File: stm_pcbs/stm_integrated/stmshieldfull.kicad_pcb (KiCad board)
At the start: 2 copper layers, 177 parts, among them P1 BNC, P2 BNC, P3 BNC, P4 BNC, P5 BNC, U1 AD8676, U10 AD8676, U11 AD5791, U12 AD8675, U13 AD8676, U14 AD8675, U15 ADR445, U16 LT1019ACS8, U17 LTC1859, U2 AD5791, U3 AD8675, U4 AD8676, U5 AD5791, U6 AD8675, U7 AD8676, U8 AD5791, U9 AD8675

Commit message: working on Kicad of 3rd Dec
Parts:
- added P6: CONN_20X2, Connectors_IDC:IDC-Header_2x20_Pitch2.54mm_Straight, F.Cu at (127.8, 64.2)
- moved U9 73.9 mm to (-17.3, 158.7)
- moved C7 73.9 mm to (-41.3, 154.8)
- moved U8 73.9 mm to (-15.0, 148.4)
- moved C12 73.9 mm to (-37.6, 147.6)
- moved P3 73.9 mm to (-24.8, 157.8)
- moved R1 73.9 mm to (-41.3, 148.4)
- moved C71 61.8 mm to (209.9, 65.8)
- moved C73 61.8 mm to (208.9, 61.8)
- moved R6 61.8 mm to (203.9, 67.8)
- moved R9 61.8 mm to (195.9, 90.0)
- moved C65 61.8 mm to (201.9, 89.8)
- moved C66 61.8 mm to (189.9, 83.8)
- moved C67 61.8 mm to (204.9, 88.8)
- moved C68 61.8 mm to (185.9, 82.8)
- moved C69 61.8 mm to (198.4, 71.3)
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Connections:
- C10 pad 2: -14V -> Net-(C10-Pad2)
- C14 pad 2: -14V -> Net-(C14-Pad2)
- C16 pad 1: -14V -> Net-(C16-Pad1)
- C18 pad 1: 3.3V -> Net-(C18-Pad1)
- C19 pad 2: +14V -> Net-(C19-Pad2)
- C2 pad 1: 3.3V -> Net-(C2-Pad1)
- C25 pad 1: +14V -> Net-(C25-Pad1)
- C25 pad 2: AGND -> Net-(C25-Pad2)
- C26 pad 2: -14V -> Net-(C26-Pad2)
- C3 pad 2: +14V -> Net-(C3-Pad2)
- C30 pad 2: -14V -> Net-(C30-Pad2)
- C32 pad 1: -14V -> Net-(C32-Pad1)
- C34 pad 1: 3.3V -> Net-(C34-Pad1)
- C35 pad 2: +14V -> Net-(C35-Pad2)
- C41 pad 1: +14V -> Net-(C41-Pad1)
- C41 pad 2: AGND -> Net-(C41-Pad2)
- C42 pad 2: -14V -> Net-(C42-Pad2)
- C46 pad 2: -14V -> Net-(C46-Pad2)
- C48 pad 1: -14V -> Net-(C48-Pad1)
- C50 pad 1: 3.3V -> Net-(C50-Pad1)
- C51 pad 2: +14V -> Net-(C51-Pad2)
- C57 pad 1: +14V -> Net-(C57-Pad1)
- C57 pad 2: AGND -> Net-(C57-Pad2)
- C58 pad 2: -14V -> Net-(C58-Pad2)
- C62 pad 2: -14V -> Net-(C62-Pad2)
- C64 pad 1: -14V -> Net-(C64-Pad1)
- C71 pad 2: -14V -> Net-(C71-Pad2)
- C72 pad 1: +14V -> Net-(C72-Pad1)
- C72 pad 2: AGND -> Net-(C72-Pad2)
- C74 pad 1: +15V -> Net-(C74-Pad1)
- C74 pad 2: GND -> DGND
- C75 pad 2: GND -> Net-(C75-Pad2)
- C76 pad 2: GND -> Net-(C76-Pad2)
- C80 pad 2: AGND -> Net-(C80-Pad2)
- C81 pad 1: +5V -> Net-(C81-Pad1)
- C82 pad 1: +5V -> Net-(C82-Pad1)
- C9 pad 1: +14V -> Net-(C9-Pad1)
- C9 pad 2: AGND -> Net-(C9-Pad2)
- P5 pad 1: Net-(C78-Pad1) -> Net-(P5-Pad1)
- R10 pad 2: AGND -> Net-(R10-Pad2)
- R5 pad 1: Net-(C69-Pad1) -> Net-(R5-Pad1)
- R5 pad 2: 5VREF -> Net-(R5-Pad2)
- R8 pad 1: +10VREF -> Net-(R8-Pad1)
- R8 pad 2: Net-(R6-Pad1) -> Net-(R8-Pad2)
- R9 pad 1: -10VREF -> Net-(R9-Pad1)
- R9 pad 2: Net-(R7-Pad1) -> Net-(R9-Pad2)
- U11 pad 14: (no net) -> SYNC4
- U11 pad 6: (no net) -> RESET4
- U11 pad 7: (no net) -> CLR4
- U11 pad 8: (no net) -> LDAC4
- U13 pad 1: Net-(R7-Pad2) -> Net-(U13-Pad1)
- U13 pad 2: Net-(R7-Pad2) -> Net-(U13-Pad1)
- U13 pad 3: Net-(C69-Pad1) -> Net-(U13-Pad3)
- U13 pad 6: Net-(R7-Pad1) -> Net-(U13-Pad6)
- U14 pad 3: Net-(C69-Pad1) -> Net-(U13-Pad3)
- U15 pad 1: (no net) -> Net-(U15-Pad1)
- U15 pad 3: (no net) -> Net-(U15-Pad3)
- U15 pad 4: GND -> DGND
- U15 pad 5: (no net) -> Net-(U15-Pad5)
- U15 pad 7: (no net) -> Net-(U15-Pad7)
- U15 pad 8: (no net) -> Net-(U15-Pad8)
- U16 pad 1: (no net) -> Net-(U16-Pad1)
- U16 pad 3: (no net) -> Net-(U16-Pad3)
- U16 pad 5: (no net) -> Net-(U16-Pad5)
- U16 pad 6: Net-(C79-Pad1) -> Net-(U16-Pad6)
- U16 pad 7: (no net) -> Net-(U16-Pad7)
- U16 pad 8: (no net) -> Net-(U16-Pad8)
- U17 pad 15: Net-(C79-Pad1) -> Net-(U16-Pad6)
- U17 pad 16: Net-(C80-Pad1) -> Net-(U17-Pad16)
- U17 pad 2: Net-(C78-Pad1) -> Net-(P5-Pad1)
- U17 pad 22: (no net) -> ADC_BUSY
- U17 pad 23: (no net) -> SDO
- U17 pad 25: (no net) -> SDIN
- U17 pad 26: (no net) -> SCLK
- U17 pad 27: (no net) -> ADC_RD
- U17 pad 28: (no net) -> ADC_CONVST
- U17 pad 3: (no net) -> Net-(U17-Pad3)
- U17 pad 4: (no net) -> Net-(U17-Pad4)
- U17 pad 5: (no net) -> Net-(U17-Pad5)
- U17 pad 6: (no net) -> Net-(U17-Pad6)
- U17 pad 7: (no net) -> Net-(U17-Pad7)
- U17 pad 8: (no net) -> Net-(U17-Pad8)
- U17 pad 9: (no net) -> Net-(U17-Pad9)
- U2 pad 14: (no net) -> SYNC2
- U2 pad 6: (no net) -> RESET2
- U2 pad 7: (no net) -> CLR2
- U2 pad 8: (no net) -> LDAC2
- U5 pad 14: (no net) -> SYNC1
- U5 pad 6: (no net) -> RESET1
- U5 pad 7: (no net) -> CLR1
- U5 pad 8: (no net) -> LDAC1
- U8 pad 14: (no net) -> SYNC3
- U8 pad 6: (no net) -> RESET3
- U8 pad 7: (no net) -> CLR3
- U8 pad 8: (no net) -> LDAC3
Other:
- board outline added: 148.6 x 101.3 mm

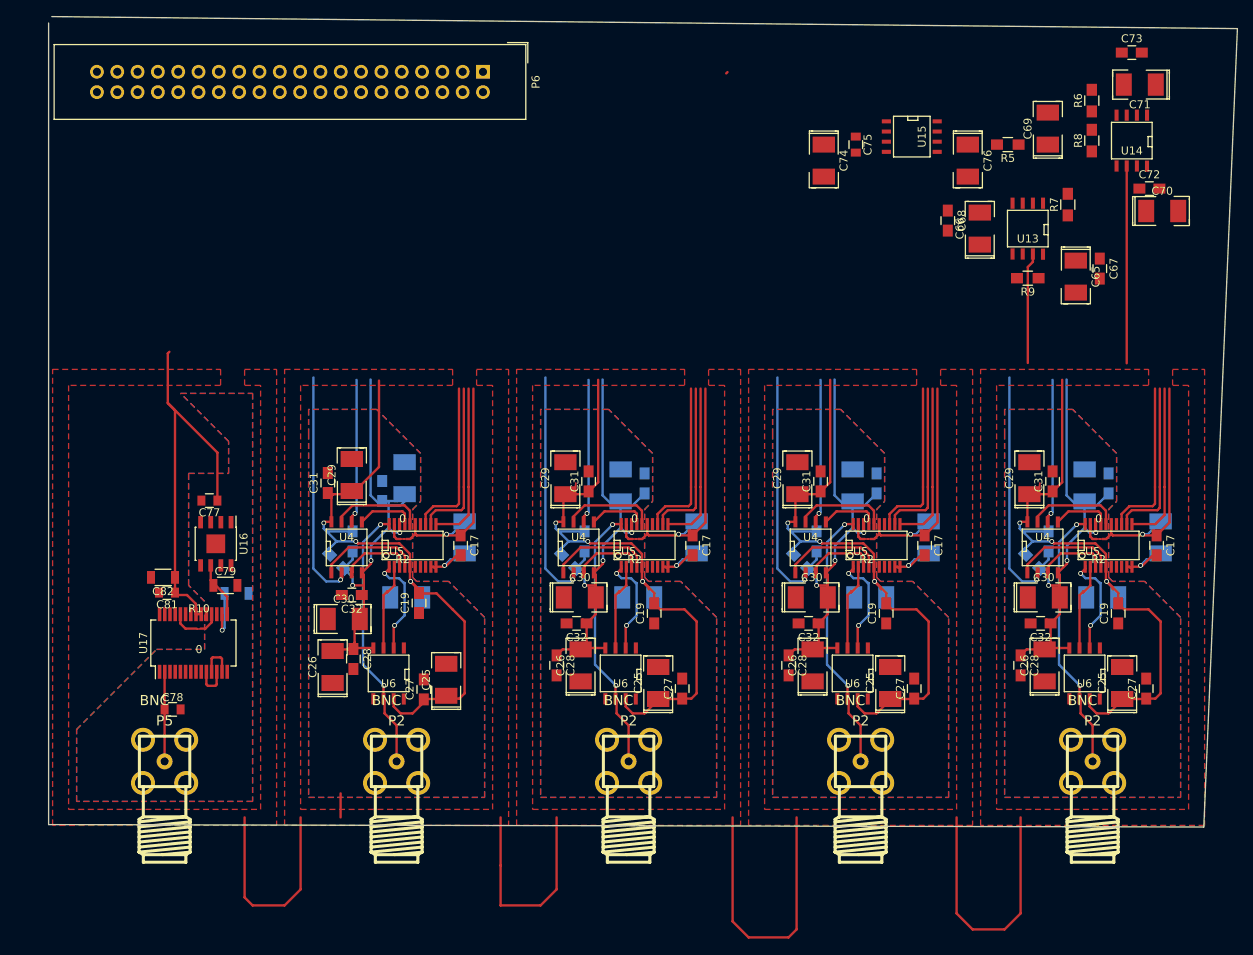
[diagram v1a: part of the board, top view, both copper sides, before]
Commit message: tidying up boards, adding all DAC signals.
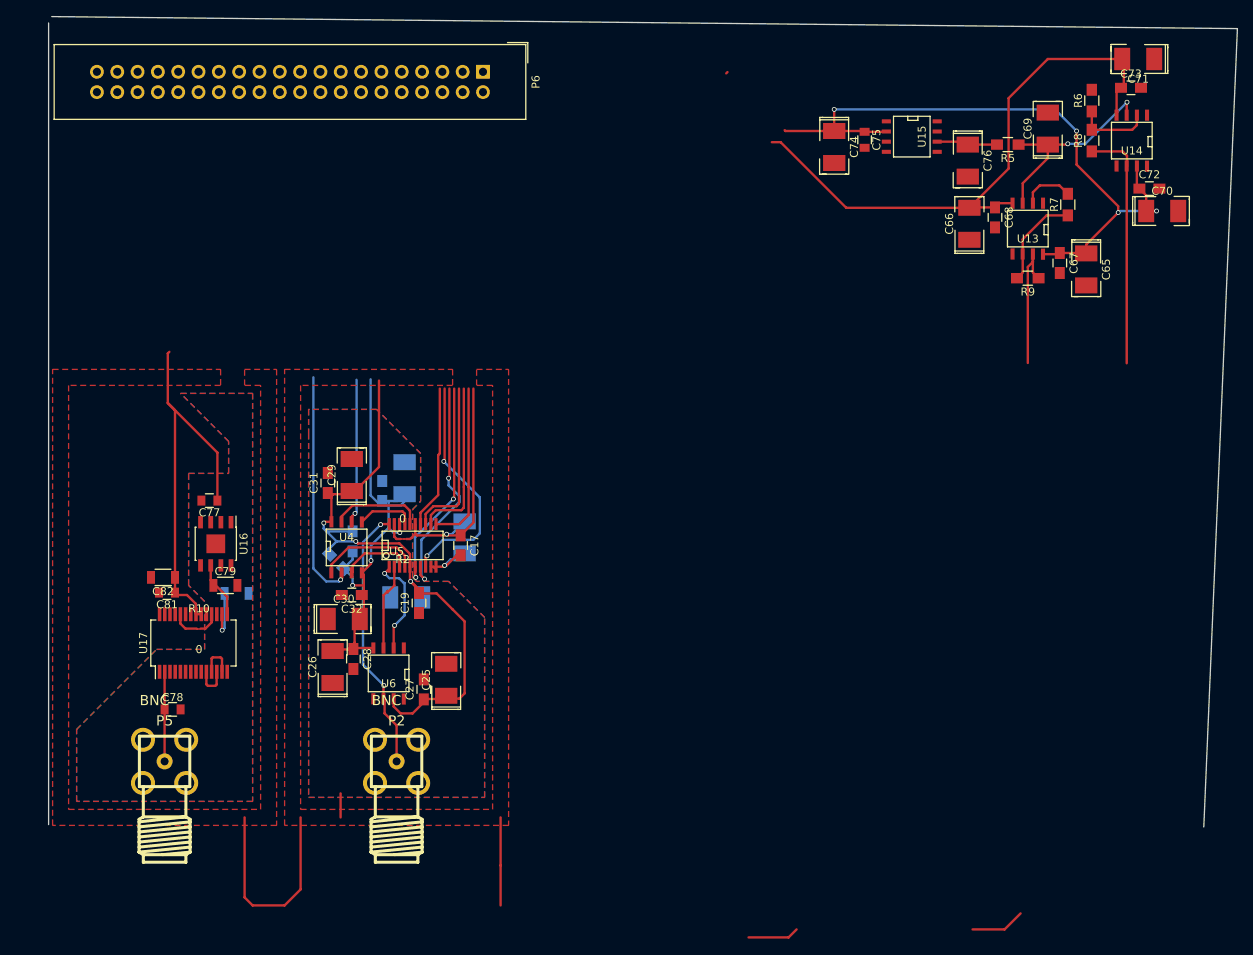
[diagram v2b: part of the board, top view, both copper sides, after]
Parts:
- removed the C17 at (183.0, 123.4)
- removed the C17 at (212.0, 123.4)
- removed the C17 at (154.0, 123.4)
- removed the C18 at (183.5, 122.4)
- removed the C18 at (212.5, 122.4)
- removed the C18 at (154.5, 122.4)
- removed the C19 at (178.2, 131.9)
- removed the C19 at (207.2, 131.9)
- removed the C19 at (149.2, 131.9)
- removed the C20 at (176.2, 129.9)
- removed the C20 at (205.2, 129.9)
- removed the C20 at (147.2, 129.9)
- removed the C21 at (177.0, 115.6)
- removed the C21 at (206.0, 115.6)
- removed the C21 at (148.0, 115.6)
- removed the C22 at (174.0, 115.9)
- removed the C22 at (203.0, 115.9)
- removed the C22 at (145.0, 115.9)
- removed the C23 at (167.5, 125.4)
- removed the C23 at (196.5, 125.4)
- removed the C23 at (138.5, 125.4)
- removed the C24 at (169.5, 122.9)
- removed the C24 at (198.5, 122.9)
- removed the C24 at (140.5, 122.9)
- removed the C25 at (178.7, 140.6)
- removed the C25 at (207.7, 140.6)
- removed the C25 at (149.7, 140.6)
- removed the C26 at (169.0, 138.4)
- removed the C26 at (198.0, 138.4)
- removed the C26 at (140.0, 138.4)
- removed the C27 at (181.7, 141.3)
- removed the C27 at (210.7, 141.3)
- removed the C27 at (152.7, 141.3)
- removed the C28 at (166.0, 138.4)
- removed the C28 at (195.0, 138.4)
- removed the C28 at (137.0, 138.4)
- removed the C29 at (167.1, 115.0)
- removed the C29 at (196.1, 115.0)
- removed the C29 at (138.1, 115.0)
- removed the C30 at (168.9, 129.9)
- removed the C30 at (197.9, 129.9)
- removed the C30 at (139.9, 129.9)
- removed the C31 at (170.0, 115.4)
- removed the C31 at (199.0, 115.4)
- removed the C31 at (141.0, 115.4)
- removed the C32 at (168.5, 133.1)
- removed the C32 at (197.5, 133.1)
- removed the C32 at (139.5, 133.1)
- removed the P2 at (175.0, 150.4)
- removed the P2 at (204.0, 150.4)
- removed the P2 at (146.0, 150.4)
- removed the R2 at (175.7, 122.6)
- removed the R2 at (204.7, 122.6)
- removed the R2 at (146.7, 122.6)
- removed the U4 at (168.7, 123.6)
- removed the U4 at (197.7, 123.6)
- removed the U4 at (139.7, 123.6)
- removed the U5 at (177.0, 123.4)
- removed the U5 at (206.0, 123.4)
- removed the U5 at (148.0, 123.4)
- removed the U6 at (174.0, 139.4)
- removed the U6 at (203.0, 139.4)
- removed the U6 at (145.0, 139.4)
- moved C68 5.91 mm to (191.8, 82.4)
- moved C67 5.05 mm to (199.9, 88.1)
- moved C73 4.40 mm to (208.8, 66.2)
- moved C71 3.21 mm to (209.7, 62.6)
- moved C74 2.14 mm to (171.7, 73.6)
- moved C65 1.58 mm to (203.2, 88.9)
- moved C66 1.43 mm to (188.6, 83.2)
- moved C75 1.25 mm to (175.5, 72.7)
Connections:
- C1 pad 2: 3.3V -> +5V
- C10 pad 2: Net-(C10-Pad2) -> -14V
- C14 pad 2: Net-(C14-Pad2) -> -14V
- C16 pad 1: Net-(C16-Pad1) -> -14V
- C17 pad 2: 3.3V -> +5V
- C18 pad 1: 3.3V -> +5V
- C2 pad 1: Net-(C2-Pad1) -> +5V
- C3 pad 2: Net-(C3-Pad2) -> +14V
- C30 pad 2: -14V -> Net-(C30-Pad2)
- C32 pad 1: -14V -> Net-(C32-Pad1)
- C33 pad 2: 3.3V -> +5V
- C34 pad 1: Net-(C34-Pad1) -> +5V
- C35 pad 2: Net-(C35-Pad2) -> +14V
- C41 pad 1: Net-(C41-Pad1) -> +14V
- C41 pad 2: Net-(C41-Pad2) -> AGND
- C42 pad 2: Net-(C42-Pad2) -> -14V
- C46 pad 2: Net-(C46-Pad2) -> -14V
- C48 pad 1: Net-(C48-Pad1) -> -14V
- C49 pad 2: 3.3V -> +5V
- C50 pad 1: Net-(C50-Pad1) -> +5V
- C51 pad 2: Net-(C51-Pad2) -> +14V
- C57 pad 1: Net-(C57-Pad1) -> +14V
- C57 pad 2: Net-(C57-Pad2) -> AGND
- C58 pad 2: Net-(C58-Pad2) -> -14V
- C62 pad 2: Net-(C62-Pad2) -> -14V
- C64 pad 1: Net-(C64-Pad1) -> -14V
- C71 pad 2: Net-(C71-Pad2) -> -14V
- C72 pad 1: Net-(C72-Pad1) -> +14V
- C72 pad 2: Net-(C72-Pad2) -> AGND
- C74 pad 1: Net-(C74-Pad1) -> +14V
- C74 pad 2: DGND -> AGND
- C75 pad 1: +15V -> +14V
- C75 pad 2: Net-(C75-Pad2) -> AGND
- C76 pad 2: Net-(C76-Pad2) -> AGND
- C80 pad 2: Net-(C80-Pad2) -> AGND
- C81 pad 1: Net-(C81-Pad1) -> +5V
- C82 pad 1: Net-(C82-Pad1) -> +5V
- C9 pad 1: Net-(C9-Pad1) -> +14V
- C9 pad 2: Net-(C9-Pad2) -> AGND
- P5 pad 1: Net-(P5-Pad1) -> Net-(C78-Pad1)
- R10 pad 2: Net-(R10-Pad2) -> AGND
- R5 pad 1: Net-(R5-Pad1) -> Net-(C69-Pad1)
- R5 pad 2: Net-(R5-Pad2) -> 5VREF
- R8 pad 1: Net-(R8-Pad1) -> +10VREF
- R8 pad 2: Net-(R8-Pad2) -> Net-(R6-Pad1)
- R9 pad 1: Net-(R9-Pad1) -> -10VREF
- R9 pad 2: Net-(R9-Pad2) -> Net-(R7-Pad1)
- U11 pad 10: 3.3V -> +5V
- U11 pad 9: 3.3V -> +5V
- U13 pad 1: Net-(U13-Pad1) -> Net-(R7-Pad2)
- U13 pad 2: Net-(U13-Pad1) -> Net-(R7-Pad2)
- U13 pad 3: Net-(U13-Pad3) -> Net-(C69-Pad1)
- U13 pad 6: Net-(U13-Pad6) -> Net-(R7-Pad1)
- U14 pad 3: Net-(U13-Pad3) -> Net-(C69-Pad1)
- U15 pad 2: +15V -> +14V
- U15 pad 4: DGND -> AGND
- U16 pad 6: Net-(U16-Pad6) -> Net-(C79-Pad1)
- U17 pad 15: Net-(U16-Pad6) -> Net-(C79-Pad1)
- U17 pad 16: Net-(U17-Pad16) -> Net-(C80-Pad1)
- U17 pad 2: Net-(P5-Pad1) -> Net-(C78-Pad1)
- U2 pad 10: 3.3V -> +5V
- U2 pad 9: 3.3V -> +5V
- U5 pad 10: 3.3V -> +5V
- U5 pad 14: (no net) -> SYNC1
- U5 pad 6: (no net) -> RESET1
- U5 pad 7: (no net) -> CLR1
- U5 pad 8: (no net) -> LDAC1
- U5 pad 9: 3.3V -> +5V
- U8 pad 10: 3.3V -> +5V
- U8 pad 9: 3.3V -> +5V
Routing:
- net +14V: track 317.4 -> 163.7 mm, vias 12 -> 7
- net -14V: track 237.6 -> 135.6 mm, vias 12 -> 3
- net Net-(P2-Pad1): track 133.5 -> 33.4 mm, vias 8 -> 2
- net DGND: track 125.1 -> 33.9 mm, vias 4 -> 1
- net +10VREF: track 140.8 -> 59.8 mm, vias 4 -> 1
- net (no net): track 128.0 -> 54.5 mm
- net SDIN: track 82.1 -> 20.5 mm
- net SCLK: track 81.4 -> 20.4 mm
- net SDO: track 81.4 -> 20.3 mm
- net -10VREF: track 86.0 -> 35.2 mm, vias 4 -> 1
- net Net-(U4-Pad1): track 51.7 -> 12.9 mm
- net Net-(U5-Pad1): track 51.0 -> 12.8 mm, vias 8 -> 2
- net Net-(U4-Pad7): track 47.0 -> 11.8 mm
- net Net-(U5-Pad2): track 44.1 -> 11.0 mm
- net LDAC1: track 0.00 -> 29.2 mm, vias 0 -> 2
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
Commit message: Using LTZ1000 (A9 board)
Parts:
- removed C1, C11, C12, C15, C16, C3, C33, C35, C37, C39, C40, C43, C44, C47, C48, C49, C5, C51, C53, C55, C56, C59, C60, C63, C64, C7, C8: 0.1uF, Capacitors_SMD:C_0805_HandSoldering
- removed C10, C13, C14, C2, C34, C36, C38, C4, C41, C42, C45, C46, C50, C52, C54, C57, C58, C6, C61, C62, C74, C9: 10uF, stm:SMD-1210_Pol
- removed C75: 0.1uF, Capacitors_SMD:C_0805
- removed C76: 0.1uF, stm:SMD-1210_Pol
- removed P1, P3, P4: BNC, stm:SMA
- removed R1, R3, R4: 0, stm:0Ohm
- removed U1, U10, U7: AD8676, stm:SOIC-8
- removed U12, U3, U9: AD8675, stm:SOIC-8
- added C17: 0.1uF, Capacitors_SMD:C_0805_HandSoldering, F.Cu at (212.0, 123.4)
- added C17: 0.1uF, Capacitors_SMD:C_0805_HandSoldering, F.Cu at (183.0, 123.4)
- added C17: 0.1uF, Capacitors_SMD:C_0805_HandSoldering, F.Cu at (154.0, 123.4)
- added C18: 10uF, stm:SMD-1210_Pol, B.Cu at (212.5, 122.4)
- added C18: 10uF, stm:SMD-1210_Pol, B.Cu at (183.5, 122.4)
- added C18: 10uF, stm:SMD-1210_Pol, B.Cu at (154.5, 122.4)
- added C19: 0.1uF, Capacitors_SMD:C_0805_HandSoldering, F.Cu at (206.8, 130.6)
- added C19: 0.1uF, Capacitors_SMD:C_0805_HandSoldering, F.Cu at (177.8, 130.6)
- added C19: 0.1uF, Capacitors_SMD:C_0805_HandSoldering, F.Cu at (148.8, 130.6)
- added C20: 10uF, stm:SMD-1210_Pol, B.Cu at (205.2, 129.9)
- added C20: 10uF, stm:SMD-1210_Pol, B.Cu at (176.2, 129.9)
- added C20: 10uF, stm:SMD-1210_Pol, B.Cu at (147.2, 129.9)
- added C21: 0.1uF, Capacitors_SMD:C_0805_HandSoldering, B.Cu at (202.2, 116.6)
- added C21: 0.1uF, Capacitors_SMD:C_0805_HandSoldering, B.Cu at (173.2, 116.6)
- added C21: 0.1uF, Capacitors_SMD:C_0805_HandSoldering, B.Cu at (144.2, 116.6)
- added C22: 10uF, stm:SMD-1210_Pol, B.Cu at (205.0, 115.0)
- added C22: 10uF, stm:SMD-1210_Pol, B.Cu at (176.0, 115.0)
- added C22: 10uF, stm:SMD-1210_Pol, B.Cu at (147.0, 115.0)
- added C23: 0.1uF, Capacitors_SMD:C_0805_HandSoldering, B.Cu at (196.5, 125.4)
- added C23: 0.1uF, Capacitors_SMD:C_0805_HandSoldering, B.Cu at (167.5, 125.4)
- added C23: 0.1uF, Capacitors_SMD:C_0805_HandSoldering, B.Cu at (138.5, 125.4)
- added C24: 0.1uF, Capacitors_SMD:C_0805_HandSoldering, B.Cu at (198.5, 122.9)
- added C24: 0.1uF, Capacitors_SMD:C_0805_HandSoldering, B.Cu at (169.5, 122.9)
- added C24: 0.1uF, Capacitors_SMD:C_0805_HandSoldering, B.Cu at (140.5, 122.9)
- added C25: 10uF, stm:SMD-1210_Pol, F.Cu at (210.2, 140.2)
- added C25: 10uF, stm:SMD-1210_Pol, F.Cu at (181.2, 140.2)
- added C25: 10uF, stm:SMD-1210_Pol, F.Cu at (152.2, 140.2)
- added C26: 10uF, stm:SMD-1210_Pol, F.Cu at (196.0, 138.6)
- added C26: 10uF, stm:SMD-1210_Pol, F.Cu at (167.0, 138.6)
- added C26: 10uF, stm:SMD-1210_Pol, F.Cu at (138.0, 138.6)
- added C27: 0.1uF, Capacitors_SMD:C_0805_HandSoldering, F.Cu at (207.4, 141.4)
- added C27: 0.1uF, Capacitors_SMD:C_0805_HandSoldering, F.Cu at (178.4, 141.4)
- added C27: 0.1uF, Capacitors_SMD:C_0805_HandSoldering, F.Cu at (149.4, 141.4)
- added C28: 0.1uF, Capacitors_SMD:C_0805_HandSoldering, F.Cu at (198.6, 137.6)
- added C28: 0.1uF, Capacitors_SMD:C_0805_HandSoldering, F.Cu at (169.6, 137.6)
- added C28: 0.1uF, Capacitors_SMD:C_0805_HandSoldering, F.Cu at (140.6, 137.6)
- added C29: 10uF, stm:SMD-1210_Pol, F.Cu at (198.4, 114.6)
- added C29: 10uF, stm:SMD-1210_Pol, F.Cu at (169.4, 114.6)
- added C29: 10uF, stm:SMD-1210_Pol, F.Cu at (140.4, 114.6)
- added C30: 10uF, stm:SMD-1210_Pol, F.Cu at (197.4, 132.6)
- added C30: 10uF, stm:SMD-1210_Pol, F.Cu at (168.4, 132.6)
- added C30: 10uF, stm:SMD-1210_Pol, F.Cu at (139.4, 132.6)
- added C31: 0.1uF, Capacitors_SMD:C_0805_HandSoldering, F.Cu at (195.4, 115.6)
- added C31: 0.1uF, Capacitors_SMD:C_0805_HandSoldering, F.Cu at (166.4, 115.6)
- added C31: 0.1uF, Capacitors_SMD:C_0805_HandSoldering, F.Cu at (137.4, 115.6)
- added C32: 0.1uF, Capacitors_SMD:C_0805_HandSoldering, F.Cu at (198.4, 129.6)
- added C32: 0.1uF, Capacitors_SMD:C_0805_HandSoldering, F.Cu at (169.4, 129.6)
- added C32: 0.1uF, Capacitors_SMD:C_0805_HandSoldering, F.Cu at (140.4, 129.6)
- added P2: BNC, stm:SMA, F.Cu at (204.0, 150.4)
- added P2: BNC, stm:SMA, F.Cu at (175.0, 150.4)
- added P2: BNC, stm:SMA, F.Cu at (146.0, 150.4)
- added R11: 0, Resistors_SMD:R_0201_NoSilk, F.Cu at (97.0, 61.4)
- added R2: 0, stm:0Ohm, F.Cu at (204.7, 122.6)
- added R2: 0, stm:0Ohm, F.Cu at (175.7, 122.6)
- added R2: 0, stm:0Ohm, F.Cu at (146.7, 122.6)
- added U4: AD8676, stm:SOIC-8, F.Cu at (197.7, 123.6)
- added U4: AD8676, stm:SOIC-8, F.Cu at (168.7, 123.6)
- added U4: AD8676, stm:SOIC-8, F.Cu at (139.7, 123.6)
- added U6: AD8675, stm:SOIC-8, F.Cu at (203.0, 139.4)
- added U6: AD8675, stm:SOIC-8, F.Cu at (174.0, 139.4)
- added U6: AD8675, stm:SOIC-8, F.Cu at (145.0, 139.4)
- R6: value 1K -> 2k5
- R7: value 1K -> 10K
- R9: value 2K -> 14K
- U15: value ADR445 -> A9_REFERENCE; footprint SMD_Packages:SOIC-8-N -> A9_REFERENCE:A9REFERENCE
- moved U11 231.7 mm to (206.0, 123.4)
- moved U2 231.3 mm to (148.0, 123.4)
- moved U8 193.6 mm to (177.0, 123.4)
- moved U15 29.3 mm to (153.7, 81.9), turned to 0 degrees
- moved C82 0.85 mm to (87.8, 126.5)
- moved C81 0.65 mm to (88.3, 128.6)
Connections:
- P6 pad 27: DGND -> GND
- P6 pad 28: Net-(P6-Pad28) -> GND
- P6 pad 32: Net-(P6-Pad32) -> +5V
- P6 pad 36: Net-(P6-Pad36) -> -14V
- P6 pad 40: Net-(P6-Pad40) -> +14V
- R5 pad 2: 5VREF -> 7VREF
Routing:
- net +14V: track 163.7 -> 739.3 mm, vias 7 -> 20
- net -14V: track 135.6 -> 683.0 mm, vias 3 -> 17
- net +5V: track 56.4 -> 419.7 mm, vias 1 -> 12
- net SCLK: track 20.4 -> 312.6 mm, vias 0 -> 10
- net -10VREF: track 35.2 -> 325.0 mm, vias 1 -> 15
- net SDO: track 20.3 -> 309.1 mm, vias 0 -> 9
- net SDIN: track 20.5 -> 301.4 mm, vias 0 -> 10
- net DGND: track 33.9 -> 283.6 mm, vias 1 -> 11
- net +10VREF: track 59.8 -> 267.2 mm, vias 1 -> 13
- net RESET3: track 0.00 -> 171.2 mm, vias 0 -> 4
- net CLR4: track 0.00 -> 158.5 mm, vias 0 -> 4
- net LDAC4: track 0.00 -> 157.7 mm, vias 0 -> 4
- net RESET4: track 0.00 -> 155.2 mm, vias 0 -> 4
- net LDAC3: track 0.00 -> 154.4 mm, vias 0 -> 4
- net SYNC4: track 0.00 -> 142.7 mm, vias 0 -> 2
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- added copper zone on B.Cu, net DGND
- added copper zone on F.Cu, net DGND
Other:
- board size 148.6 x 101.3 mm -> 150 x 122 mm
- net class Default: clearance 0.2 -> 0.19
- rule trace_clearance: 0.2 -> 0.19
